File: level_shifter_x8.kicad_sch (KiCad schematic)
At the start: 4 parts, among them U4 LSF0108RKSR

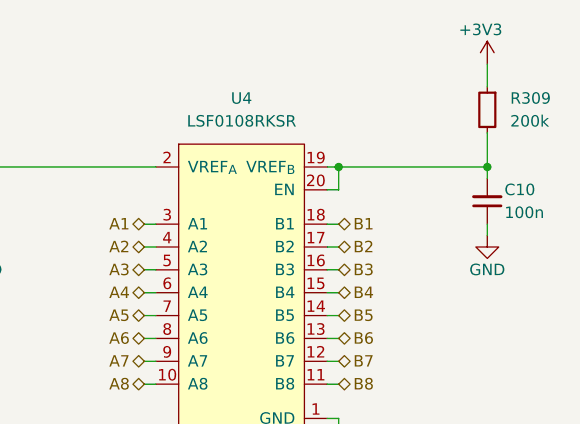
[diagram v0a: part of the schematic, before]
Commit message: [#83396] Update all symbols from library and clear all ERC errors
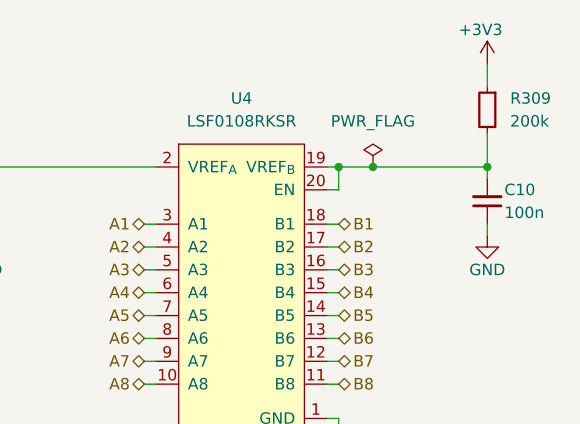
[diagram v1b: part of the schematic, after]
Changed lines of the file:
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@@
 	(paper "A4")
 	(junction
+		(at 166.37 81.28)
+		(diameter 0)
+		(color 0 0 0 0)
+	)
+	(junction
 		(at 123.19 81.28)
 		(diameter 0)
@@
 	(wire
 		(pts
-			(xy 162.56 81.28) (xy 179.07 81.28)
+			(xy 162.56 81.28) (xy 166.37 81.28)
 		)
 		(stroke
@@
 	(wire
 		(pts
+			(xy 166.37 81.28) (xy 179.07 81.28)
+		)
+		(stroke
+			(width 0)
+			(type default)
+		)
+	)
+	(wire
+		(pts
 			(xy 123.19 87.63) (xy 123.19 88.9)
 		)
@@
 			)
 		)
-		(property "Description" ""
+		(property "Description" "SMD Multilayer Ceramic Capacitor, 0.1 µF, 50 V, 0402 [1005 Metric], ± 10%, X5R, GRM Series"
 			(at 123.19 87.63 0)
 			(effects
@@
 	)
 	(symbol
+		(lib_id "antmicropower:PWR_FLAG")
+		(at 166.37 81.28 0)
+		(unit 1)
+		(exclude_from_sim no)
+		(in_bom yes)
+		(on_board yes)
+		(dnp no)
+		(fields_autoplaced yes)
+		(property "Reference" "#FLG013"
+			(at 166.37 79.375 0)
+			(effects
+				(font
+					(size 1.27 1.27)
+				)
+				(hide yes)
+			)
+		)
+		(property "Value" "PWR_FLAG"
+			(at 166.37 76.2 0)
+			(effects
+				(font
+					(size 1.27 1.27)
+				)
+			)
+		)
+		(property "Footprint" ""
+			(at 166.37 81.28 0)
+			(effects
+				(font
+					(size 1.27 1.27)
+				)
+				(hide yes)
+			)
+		)
+		(property "Datasheet" ""
+			(at 166.37 81.28 0)
+			(effects
+				(font
+					(size 1.27 1.27)
+				)
+				(hide yes)
+			)
+		)
+		(property "Description" ""
+			(at 166.37 83.82 0)
+			(effects
+				(font
+					(size 1.27 1.27)
+				)
+				(justify left bottom)
+				(hide yes)
+			)
+		)
+		(pin "1"
+		)
+		(instances
+			(project ""
+				(path "/f569b0be-0afd-48b7-93ee-28582a4c645c/5e8e155a-019a-4868-a371-a2eb1e119b3e/3abc05cd-228c-4eb8-b63c-e3ac25c2b310"
+					(reference "#FLG013")
+					(unit 1)
+				)
+				(path "/f569b0be-0afd-48b7-93ee-28582a4c645c/5e8e155a-019a-4868-a371-a2eb1e119b3e/4badc71d-812d-4df6-9069-2f39dff9a44f"
+					(reference "#FLG017")
+					(unit 1)
+				)
+				(path "/f569b0be-0afd-48b7-93ee-28582a4c645c/5e8e155a-019a-4868-a371-a2eb1e119b3e/4c6f7b17-5be9-4217-b67d-50974b1b0d52"
+					(reference "#FLG014")
+					(unit 1)
+				)
+				(path "/f569b0be-0afd-48b7-93ee-28582a4c645c/5e8e155a-019a-4868-a371-a2eb1e119b3e/75857eb3-9fe0-420d-9c74-9aac0fcec98c"
+					(reference "#FLG019")
+					(unit 1)
+				)
+				(path "/f569b0be-0afd-48b7-93ee-28582a4c645c/5e8e155a-019a-4868-a371-a2eb1e119b3e/77a48c76-1efb-4e96-8b9e-54718d63a699"
+					(reference "#FLG020")
+					(unit 1)
+				)
+				(path "/f569b0be-0afd-48b7-93ee-28582a4c645c/5e8e155a-019a-4868-a371-a2eb1e119b3e/8ce67c72-d2af-4f7d-8793-c0cab0729fb5"
+					(reference "#FLG018")
+					(unit 1)
+				)
+				(path "/f569b0be-0afd-48b7-93ee-28582a4c645c/5e8e155a-019a-4868-a371-a2eb1e119b3e/9d09b695-5288-4f42-88ad-d65175bdc122"
+					(reference "#FLG015")
+					(unit 1)
+				)
+				(path "/f569b0be-0afd-48b7-93ee-28582a4c645c/5e8e155a-019a-4868-a371-a2eb1e119b3e/cab0bc42-9bc8-4167-9bf4-c94b0dbb21ec"
+					(reference "#FLG016")
+					(unit 1)
+				)
+			)
+		)
+	)
+	(symbol
 		(lib_id "antmicropower:GND")
 		(at 162.56 113.03 0)
@@
 			)
 		)
-		(property "Description" ""
+		(property "Description" "SMD Multilayer Ceramic Capacitor, 0.1 µF, 50 V, 0402 [1005 Metric], ± 10%, X5R, GRM Series"
 			(at 179.07 87.63 0)
 			(effects

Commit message: [#83396] Implement small post review fixes eg. correct LED resistor values, update sheet table, delete four wire connections
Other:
- company: (none) -> Antmicro Ltd
- title: (none) -> Jetson AGX Thor Baseboard
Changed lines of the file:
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@@
 	(generator "eeschema")
 	(generator_version "9.0")
-	(paper "A4")
+	(paper "A3")
+	(title_block
+		(title "Jetson AGX Thor Baseboard")
+		(date "2025-08-11")
+		(rev "1.0.0")
+		(company "Antmicro Ltd")
+		(comment 1 "www.antmicro.com")
+	)
 	(junction
 		(at 166.37 81.28)
@@
 	)
 	(image
-		(at 59.2091 180)
+		(at 61.1141 271.44)
 		(scale 0.472441)
 		(data "iVBORw0KGgoAAAANSUhEUgAABLAAAAF9CAYAAAAUb5ECAABCnklEQVR4Ae3dvX4j17kv6P/22cHO"
@@
 	)
 	(image
-		(at 22.614 180)
+		(at 24.519 271.44)
 		(scale 0.15)
 		(data "iVBORw0KGgoAAAANSUhEUgAABLAAAASwCAIAAABkQySYAAAAA3NCSVQICAjb4U/gAAAACXBIWXMA"

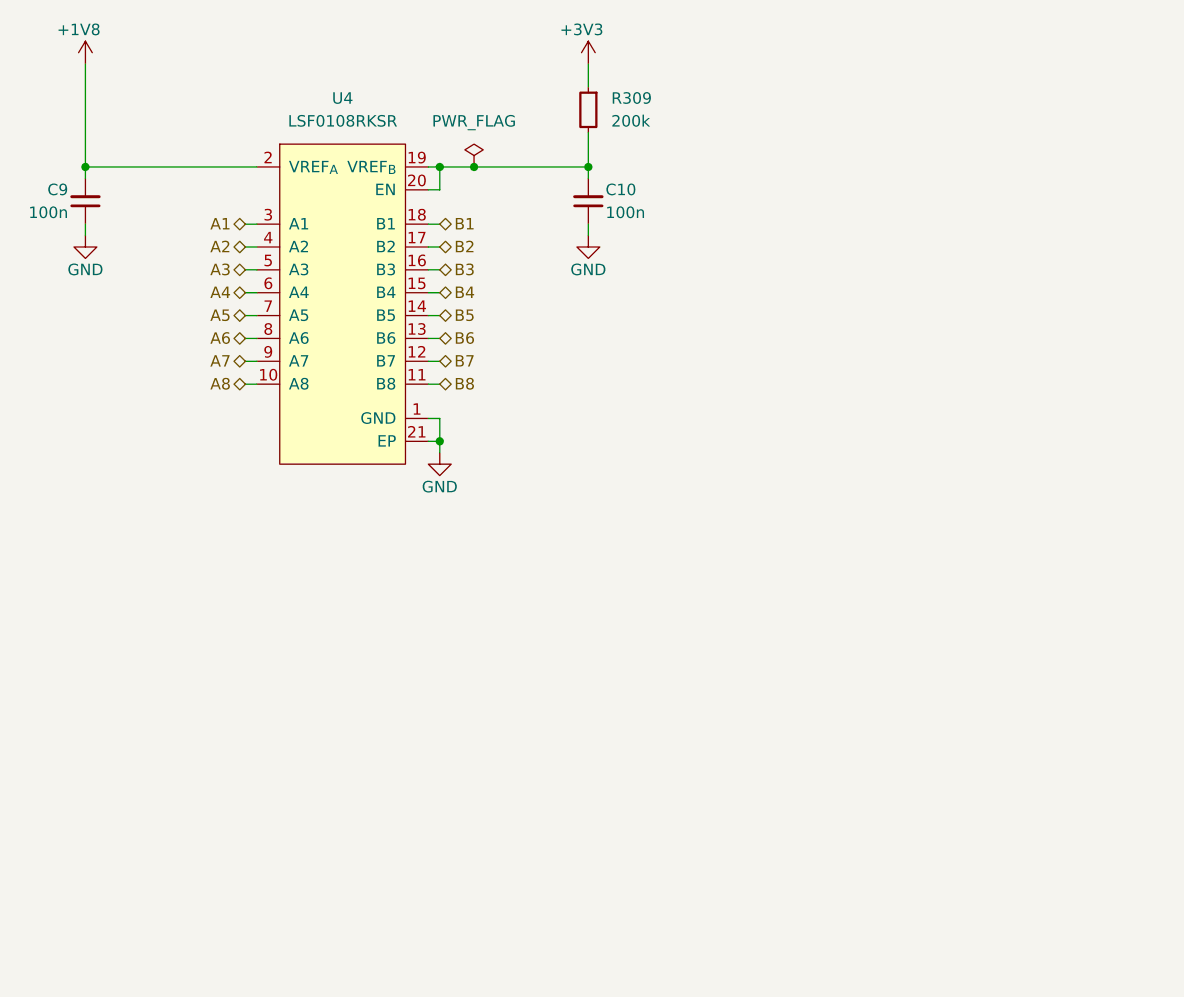
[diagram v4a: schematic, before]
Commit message: [#85326] Change SoM IO level shifters for ones with pull-ups. add pull-ups to I2C lines
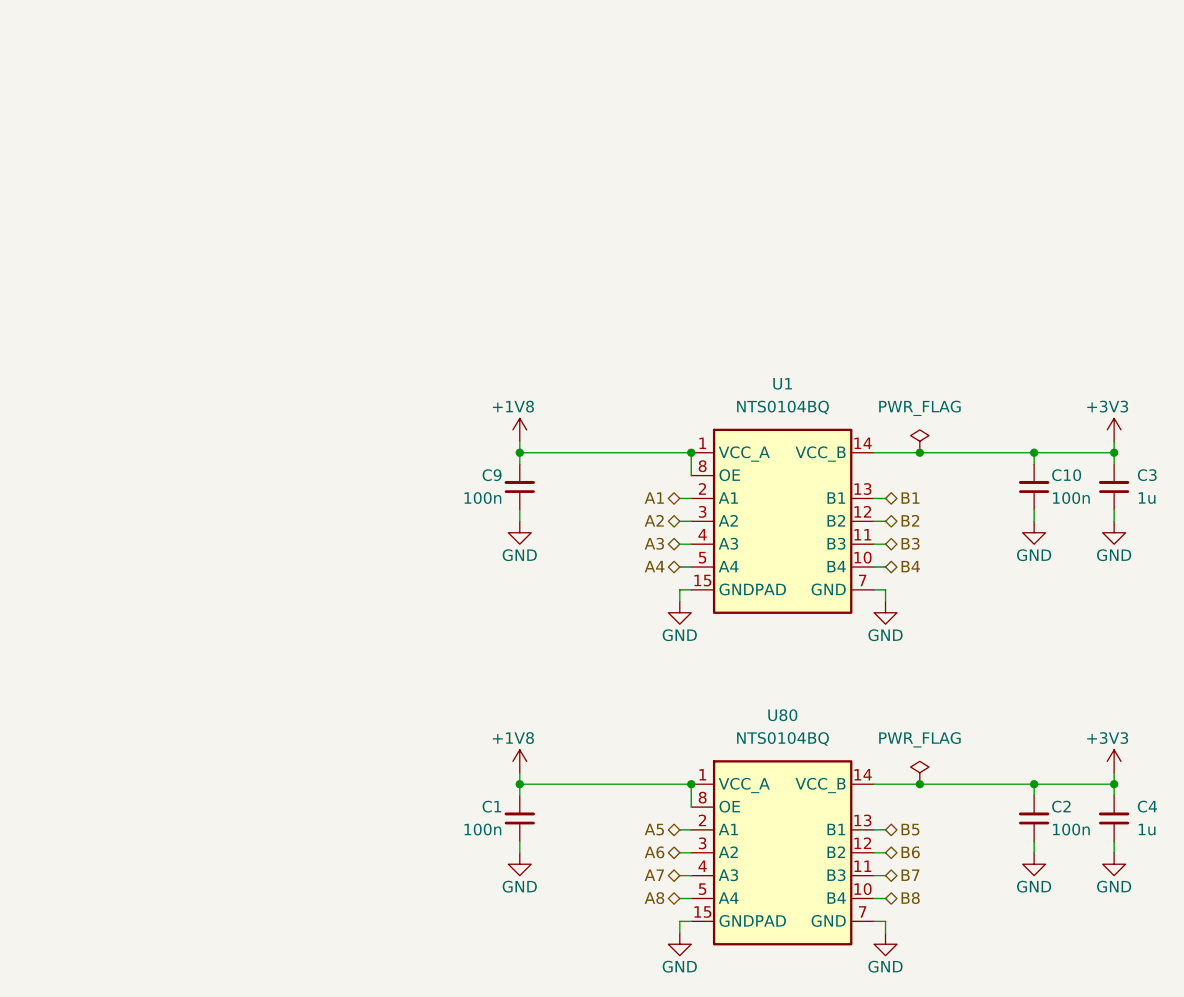
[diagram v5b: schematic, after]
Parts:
- removed R309: R_200k_0402, antmicro-footprints:R_0402_1005Metric, symbol antmicroResistors0402:R_200k_0402
- removed U4: LSF0108RKSR, antmicro-footprints:VQFN-20_1EP_4.5x2.5mm_P0.5mm, symbol antmicroLogicTranslatorsLevelShifters:LSF0108RKSR
- added C1, C2: C_100n_0402, antmicro-footprints:C_0402_1005Metric, symbol antmicroCapacitors0402:C_100n_0402
- added C3, C4: C_1u_0402, antmicro-footprints:C_0402_1005Metric, symbol antmicroCapacitors0402:C_1u_0402
- added U1, U80: NTS0104_DHVQFN, antmicro-footprints:DHVQFN-14-1EP_2.5x3mm, symbol antmicroLogicTranslatorsLevelShifters:NTS0104_DHVQFN
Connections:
- net +1V8: now also C1.2, U1.1 (VCC_A), U1.8 (OE), U80.1 (VCC_A), U80.8 (OE)
- net +3V3: now also C10.2, C2.2, C3.2, C4.2, U1.14 (VCC_B), U80.14 (VCC_B)
- net A1: now also U1.2 (A1)
- net A2: now also U1.3 (A2)
- net A3: now also U1.4 (A3)
- net A4: now also U1.5 (A4)
- net A5: now also U80.2 (A1)
- net A6: now also U80.3 (A2)
- net A7: now also U80.4 (A3)
- net A8: now also U80.5 (A4)
- net B1: now also U1.13 (B1)
- net B2: now also U1.12 (B2)
- net B3: now also U1.11 (B3)
- net B4: now also U1.10 (B4)
- net B5: now also U80.13 (B1)
- net B6: now also U80.12 (B2)
- net B7: now also U80.11 (B3)
- net B8: now also U80.10 (B4)
- net GND: now also C1.1, C2.1, C3.1, C4.1, U1.15 (GNDPAD), U1.7 (GND), U80.15 (GNDPAD), U80.7 (GND)
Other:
- moved on the sheet: C10, C9

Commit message: [#85488] Annotate sch
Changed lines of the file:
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@@
 	(title_block
 		(title "Jetson AGX Thor Baseboard")
-		(date "2025-10-16")
+		(date "2025-10-21")
 		(rev "1.0.0")
 		(company "Antmicro Ltd")
@@
 	)
 	(junction
-		(at 215.9 113.03)
-		(diameter 0)
-		(color 0 0 0 0)
-	)
-	(junction
 		(at 228.6 113.03)
 		(diameter 0)
@@
 	)
 	(junction
-		(at 215.9 149.86)
-		(diameter 0)
-		(color 0 0 0 0)
-	)
-	(junction
 		(at 190.5 149.86)
 		(diameter 0)
@@
 	(wire
 		(pts
-			(xy 210.82 113.03) (xy 215.9 113.03)
-		)
-		(stroke
-			(width 0)
-			(type default)
-		)
-	)
-	(wire
-		(pts
 			(xy 189.23 125.73) (xy 190.5 125.73)
 		)
@@
 	(wire
 		(pts
-			(xy 215.9 113.03) (xy 228.6 113.03)
+			(xy 210.82 113.03) (xy 228.6 113.03)
 		)
 		(stroke
@@
 	(wire
 		(pts
-			(xy 215.9 149.86) (xy 228.6 149.86)
-		)
-		(stroke
-			(width 0)
-			(type default)
-		)
-	)
-	(wire
-		(pts
 			(xy 212.09 128.27) (xy 210.82 128.27)
 		)
@@
 	(wire
 		(pts
-			(xy 210.82 149.86) (xy 215.9 149.86)
+			(xy 210.82 149.86) (xy 228.6 149.86)
 		)
 		(stroke
@@
 	)
 	(symbol
-		(lib_id "antmicropower:PWR_FLAG")
-		(at 215.9 113.03 0)
-		(unit 1)
-		(exclude_from_sim no)
-		(in_bom yes)
-		(on_board yes)
-		(dnp no)
-		(fields_autoplaced yes)
-		(property "Reference" "#FLG013"
-			(at 215.9 111.125 0)
-			(effects
-				(font
-					(size 1.27 1.27)
-				)
-				(hide yes)
-			)
-		)
-		(property "Value" "PWR_FLAG"
-			(at 215.9 107.95 0)
-			(effects
-				(font
-					(size 1.27 1.27)
-				)
-			)
-		)
-		(property "Footprint" ""
-			(at 215.9 113.03 0)
-			(effects
-				(font
-					(size 1.27 1.27)
-				)
-				(hide yes)
-			)
-		)
-		(property "Datasheet" ""
-			(at 215.9 113.03 0)
-			(effects
-				(font
-					(size 1.27 1.27)
-				)
-				(hide yes)
-			)
-		)
-		(property "Description" ""
-			(at 215.9 115.57 0)
-			(effects
-				(font
-					(size 1.27 1.27)
-				)
-				(justify left bottom)
-				(hide yes)
-			)
-		)
-		(pin "1"
-		)
-		(instances
-			(project "jetson-agx-thor-baseboard"
-				(path "/f569b0be-0afd-48b7-93ee-28582a4c645c/5e8e155a-019a-4868-a371-a2eb1e119b3e/3abc05cd-228c-4eb8-b63c-e3ac25c2b310"
-					(reference "#FLG013")
-					(unit 1)
-				)
-				(path "/f569b0be-0afd-48b7-93ee-28582a4c645c/5e8e155a-019a-4868-a371-a2eb1e119b3e/4badc71d-812d-4df6-9069-2f39dff9a44f"
-					(reference "#FLG0108")
-					(unit 1)
-				)
-				(path "/f569b0be-0afd-48b7-93ee-28582a4c645c/5e8e155a-019a-4868-a371-a2eb1e119b3e/4c6f7b17-5be9-4217-b67d-50974b1b0d52"
-					(reference "#FLG0102")
-					(unit 1)
-				)
-				(path "/f569b0be-0afd-48b7-93ee-28582a4c645c/5e8e155a-019a-4868-a371-a2eb1e119b3e/75857eb3-9fe0-420d-9c74-9aac0fcec98c"
-					(reference "#FLG0112")
-					(unit 1)
-				)
-				(path "/f569b0be-0afd-48b7-93ee-28582a4c645c/5e8e155a-019a-4868-a371-a2eb1e119b3e/77a48c76-1efb-4e96-8b9e-54718d63a699"
-					(reference "#FLG0114")
-					(unit 1)
-				)
-				(path "/f569b0be-0afd-48b7-93ee-28582a4c645c/5e8e155a-019a-4868-a371-a2eb1e119b3e/8ce67c72-d2af-4f7d-8793-c0cab0729fb5"
-					(reference "#FLG0110")
-					(unit 1)
-				)
-				(path "/f569b0be-0afd-48b7-93ee-28582a4c645c/5e8e155a-019a-4868-a371-a2eb1e119b3e/9d09b695-5288-4f42-88ad-d65175bdc122"
-					(reference "#FLG0104")
-					(unit 1)
-				)
-				(path "/f569b0be-0afd-48b7-93ee-28582a4c645c/5e8e155a-019a-4868-a371-a2eb1e119b3e/cab0bc42-9bc8-4167-9bf4-c94b0dbb21ec"
-					(reference "#FLG0106")
-					(unit 1)
-				)
-			)
-		)
-	)
-	(symbol
 		(lib_id "antmicroLogicTranslatorsLevelShifters:NTS0104_DHVQFN")
 		(at 190.5 113.03 0)
@@
 					(unit 1)
 				)
-			)
-		)
-	)
-	(symbol
-		(lib_id "antmicropower:PWR_FLAG")
-		(at 215.9 149.86 0)
-		(unit 1)
-		(exclude_from_sim no)
-		(in_bom yes)
-		(on_board yes)
-		(dnp no)
-		(fields_autoplaced yes)
-		(property "Reference" "#FLG08"
-			(at 215.9 147.955 0)
-			(effects
-				(font
-					(size 1.27 1.27)
-				)
-				(hide yes)
-			)
-		)
-		(property "Value" "PWR_FLAG"
-			(at 215.9 144.78 0)
-			(effects
-				(font
-					(size 1.27 1.27)
-				)
-			)
-		)
-		(property "Footprint" ""
-			(at 215.9 149.86 0)
-			(effects
-				(font
-					(size 1.27 1.27)
-				)
-				(hide yes)
-			)
-		)
-		(property "Datasheet" ""
-			(at 215.9 149.86 0)
-			(effects
-				(font
-					(size 1.27 1.27)
-				)
-				(hide yes)
-			)
-		)
-		(property "Description" ""
-			(at 215.9 152.4 0)
-			(effects
-				(font
-					(size 1.27 1.27)
-				)
-				(justify left bottom)
-				(hide yes)
-			)
-		)
-		(pin "1"
-		)
-		(instances
-			(project "jetson-agx-thor-baseboard"
-				(path "/f569b0be-0afd-48b7-93ee-28582a4c645c/5e8e155a-019a-4868-a371-a2eb1e119b3e/3abc05cd-228c-4eb8-b63c-e3ac25c2b310"
-					(reference "#FLG08")
-					(unit 1)
-				)
-				(path "/f569b0be-0afd-48b7-93ee-28582a4c645c/5e8e155a-019a-4868-a371-a2eb1e119b3e/4badc71d-812d-4df6-9069-2f39dff9a44f"
-					(reference "#FLG0107")
-					(unit 1)
-				)
-				(path "/f569b0be-0afd-48b7-93ee-28582a4c645c/5e8e155a-019a-4868-a371-a2eb1e119b3e/4c6f7b17-5be9-4217-b67d-50974b1b0d52"
-					(reference "#FLG0101")
-					(unit 1)
-				)
-				(path "/f569b0be-0afd-48b7-93ee-28582a4c645c/5e8e155a-019a-4868-a371-a2eb1e119b3e/75857eb3-9fe0-420d-9c74-9aac0fcec98c"
-					(reference "#FLG0111")
-					(unit 1)
-				)
-				(path "/f569b0be-0afd-48b7-93ee-28582a4c645c/5e8e155a-019a-4868-a371-a2eb1e119b3e/77a48c76-1efb-4e96-8b9e-54718d63a699"
-					(reference "#FLG0113")
-					(unit 1)
-				)
-				(path "/f569b0be-0afd-48b7-93ee-28582a4c645c/5e8e155a-019a-4868-a371-a2eb1e119b3e/8ce67c72-d2af-4f7d-8793-c0cab0729fb5"
-					(reference "#FLG0109")
-					(unit 1)
-				)
-				(path "/f569b0be-0afd-48b7-93ee-28582a4c645c/5e8e155a-019a-4868-a371-a2eb1e119b3e/9d09b695-5288-4f42-88ad-d65175bdc122"
-					(reference "#FLG0103")
-					(unit 1)
-				)
-				(path "/f569b0be-0afd-48b7-93ee-28582a4c645c/5e8e155a-019a-4868-a371-a2eb1e119b3e/cab0bc42-9bc8-4167-9bf4-c94b0dbb21ec"
-					(reference "#FLG0105")
-					(unit 1)
-				)

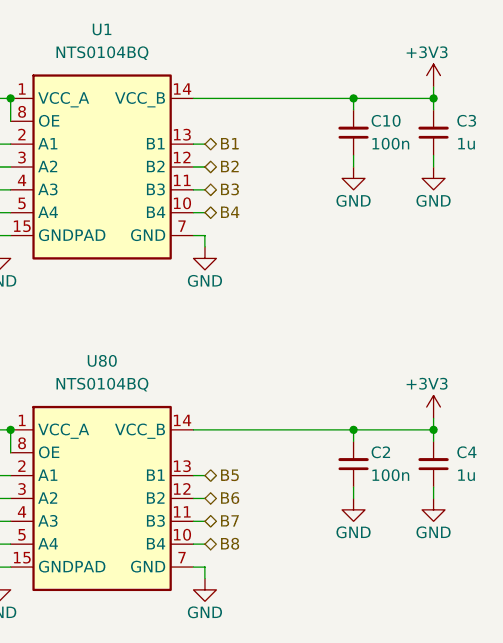
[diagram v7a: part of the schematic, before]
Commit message: [#85488] Optimize VCONN switches
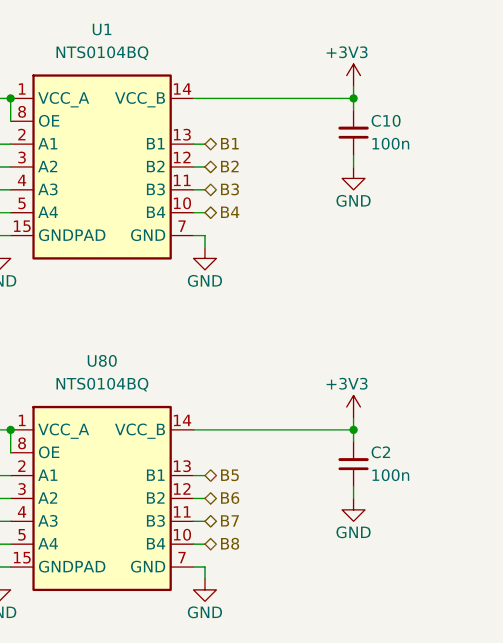
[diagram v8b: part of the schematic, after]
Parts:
- removed C3, C4: C_1u_0402, antmicro-footprints:C_0402_1005Metric, symbol antmicroCapacitors0402:C_1u_0402
